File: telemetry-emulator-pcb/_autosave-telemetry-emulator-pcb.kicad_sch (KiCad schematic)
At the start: 55 parts, among them IC1 ATmega328P, IC2 MCP2515, IC3 MCP2551, J1 USB, J2 RX_TX, J3 GPIO, J4 CAN_TERM, J5 V_INT, J6 UART, J7 CAN, J8 CAN, Q1 BSS138, Q2 BSS138, U1 CH340C, Y1 16MHz, Y2 8MHz

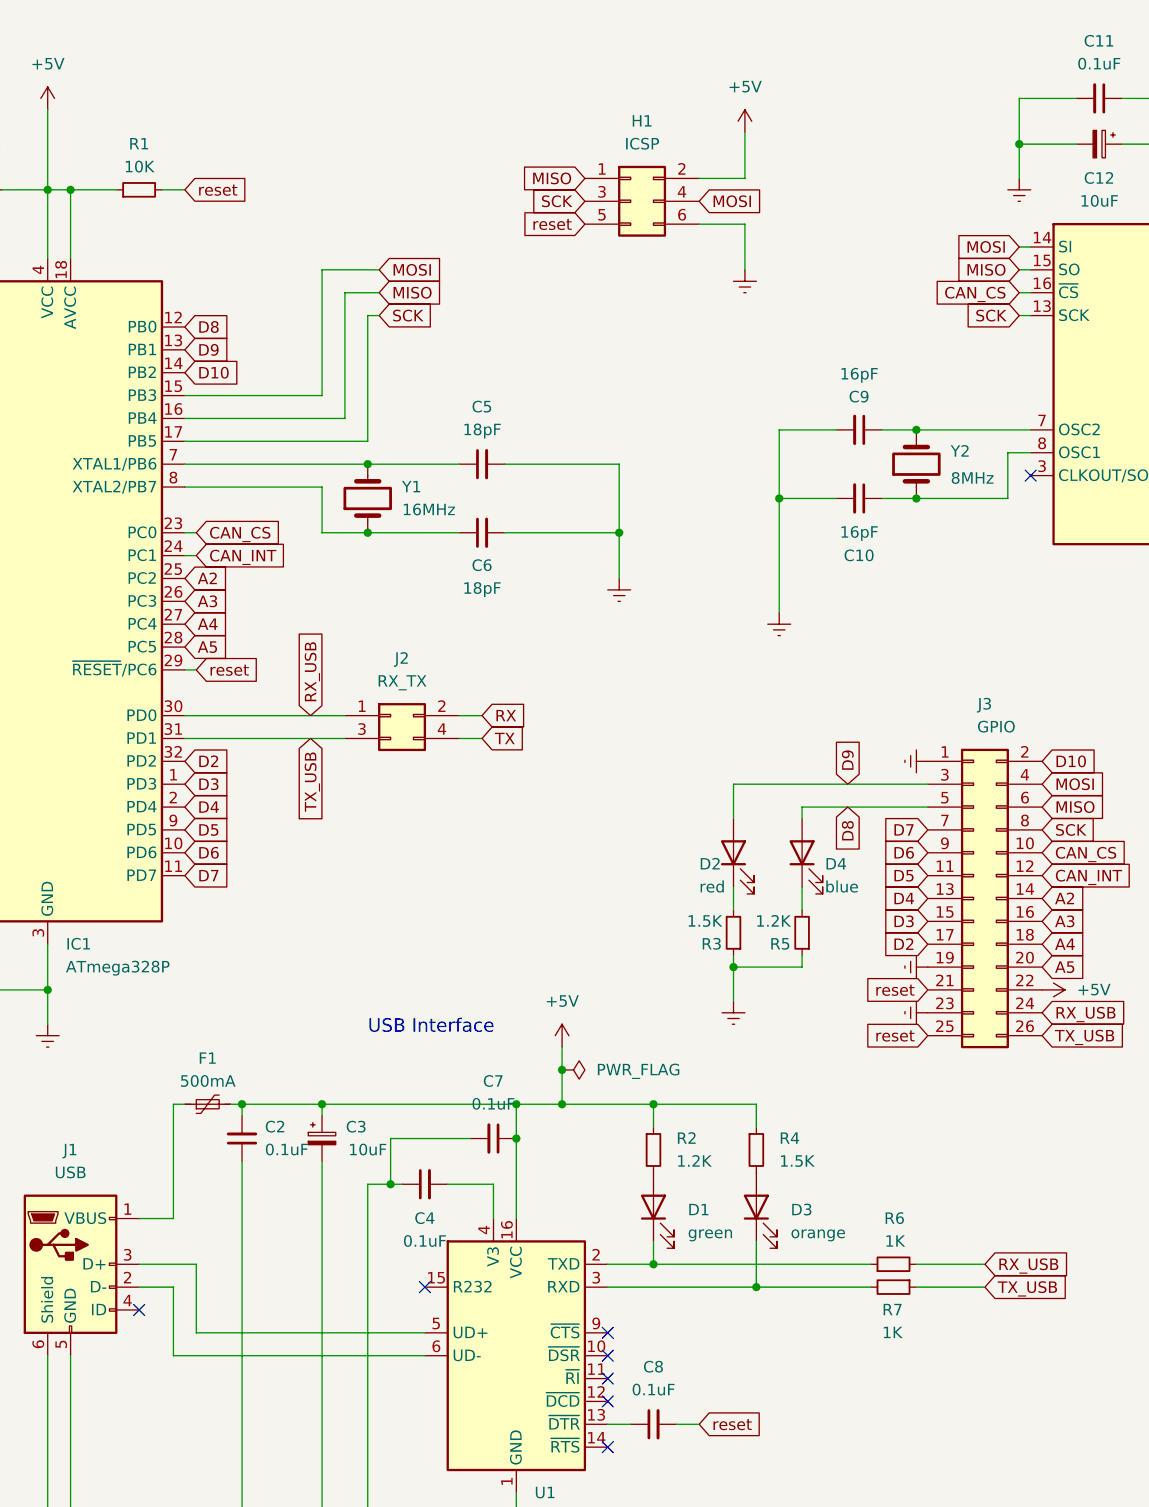
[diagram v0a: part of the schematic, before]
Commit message: Fixes reset issue
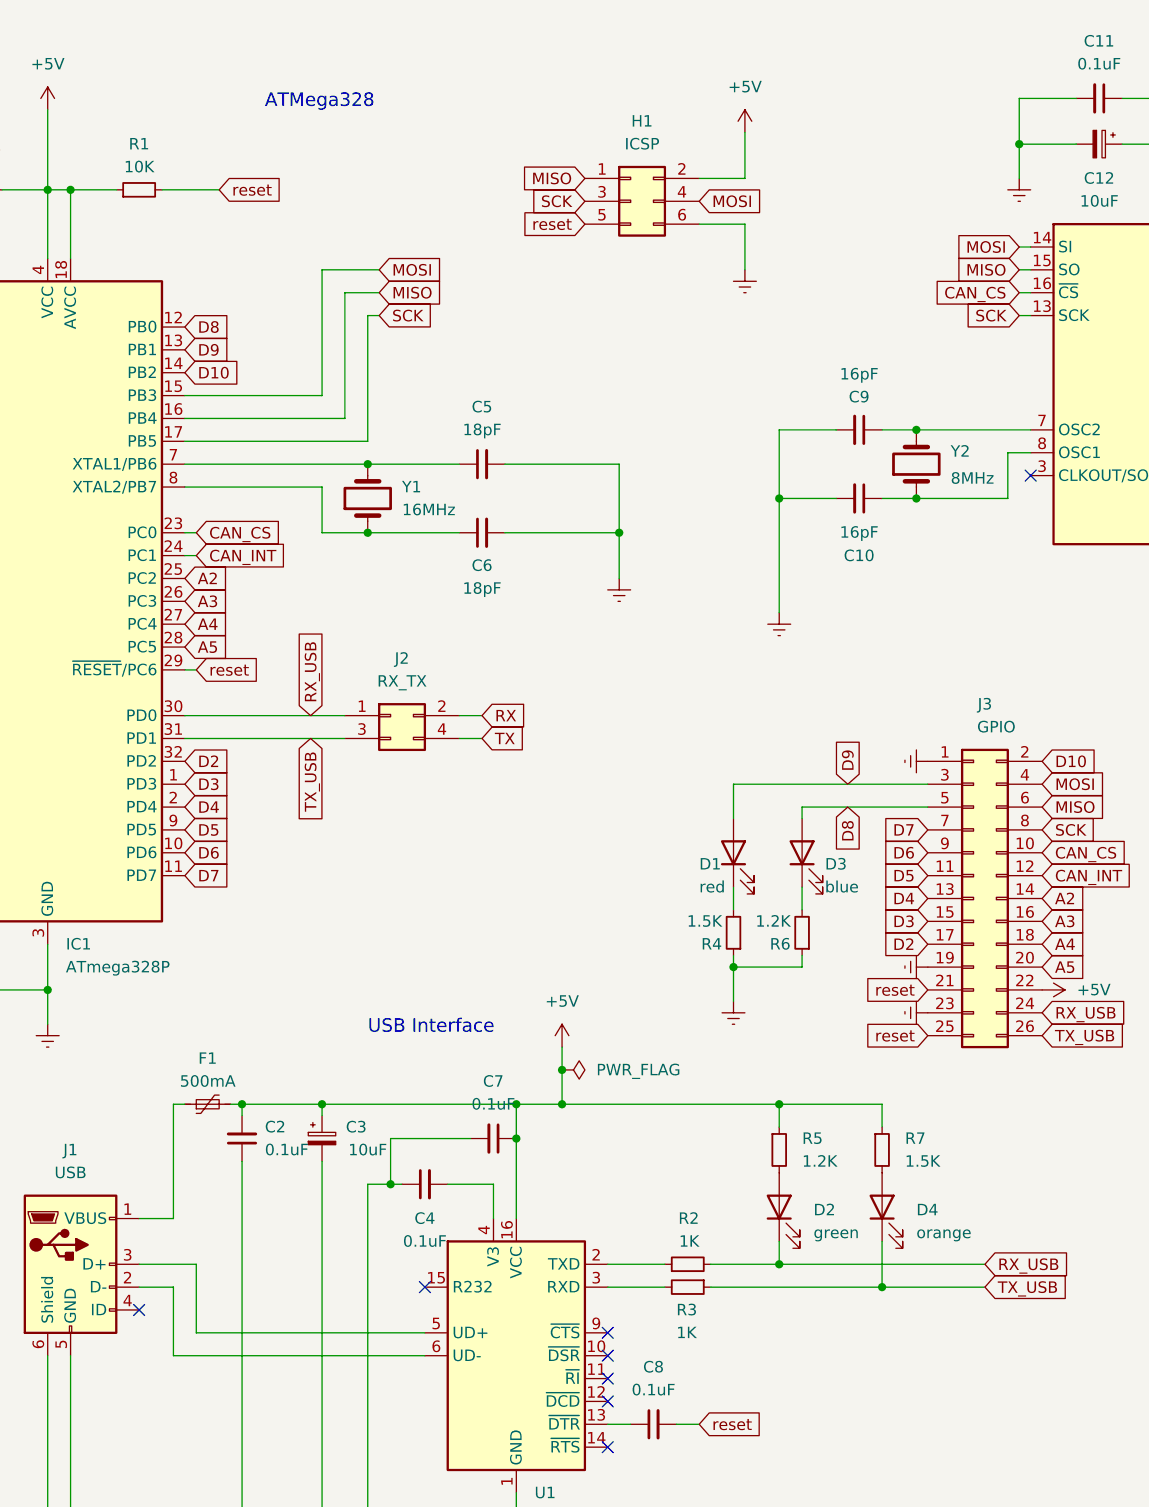
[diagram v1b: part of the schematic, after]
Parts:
- renumbered D2 to D1, D1 to D2, D4 to D3, D3 to D4, R6 to R2, R7 to R3, R3 to R4, R2 to R5, R5 to R6, R4 to R7
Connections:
- net RX_USB: now also D2.1 (K)
- net TX_USB: now also D4.1 (K)
- net at R2.1, U1.2 (TXD): no longer D2.1 (K)
- net at R3.2, U1.3 (RXD): no longer D4.1 (K)
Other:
- note added: "ATMega328"
- moved on the sheet: D2, D4, R2, R3, R5, R7
